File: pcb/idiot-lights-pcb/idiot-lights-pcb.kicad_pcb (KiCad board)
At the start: 2 copper layers, 100.3 x 66 mm, 49 parts, among them SW1 Toggle left indicator, SW2 Toggle right indicator, SW3 Toggle hazard warning, SW4 Break control, SW5 Reset, U1 RaspberryPi_Pico

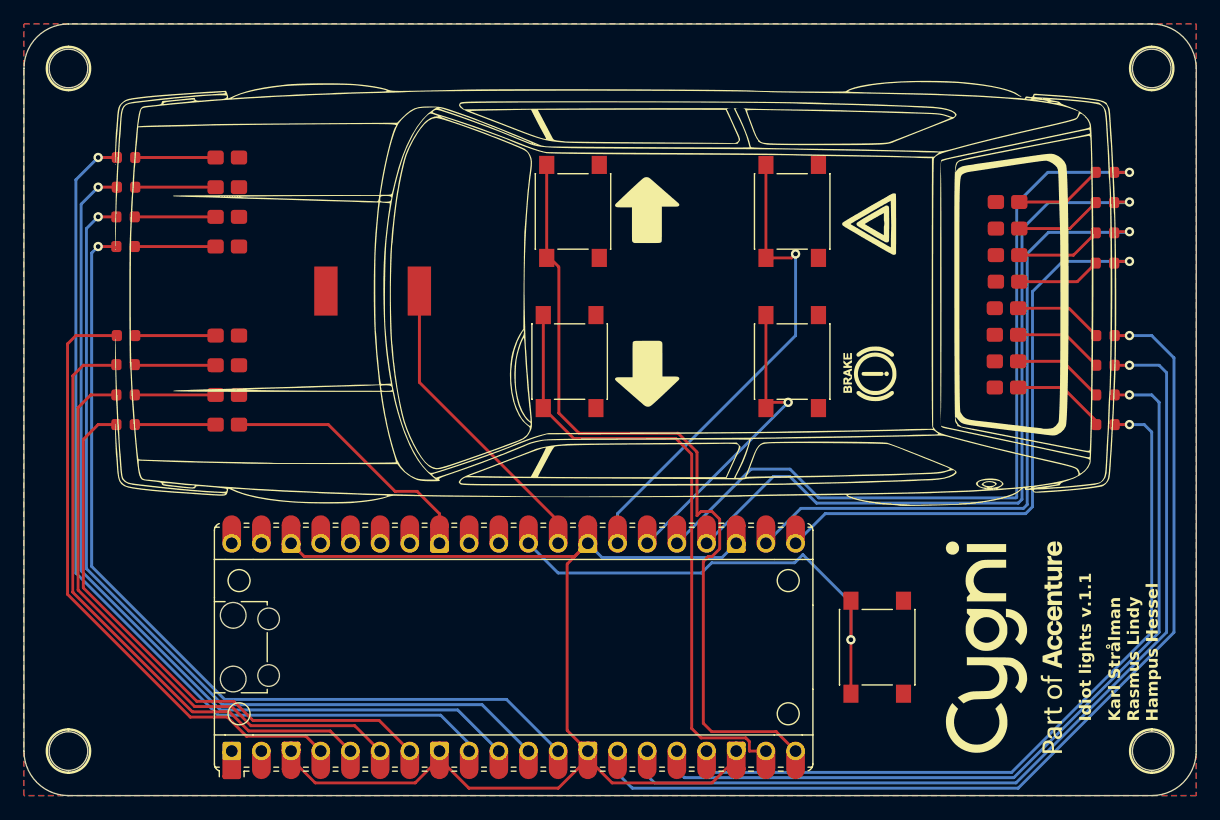
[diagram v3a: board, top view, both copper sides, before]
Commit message: Add mosfet controlling every LED and let 5V rail handle powering
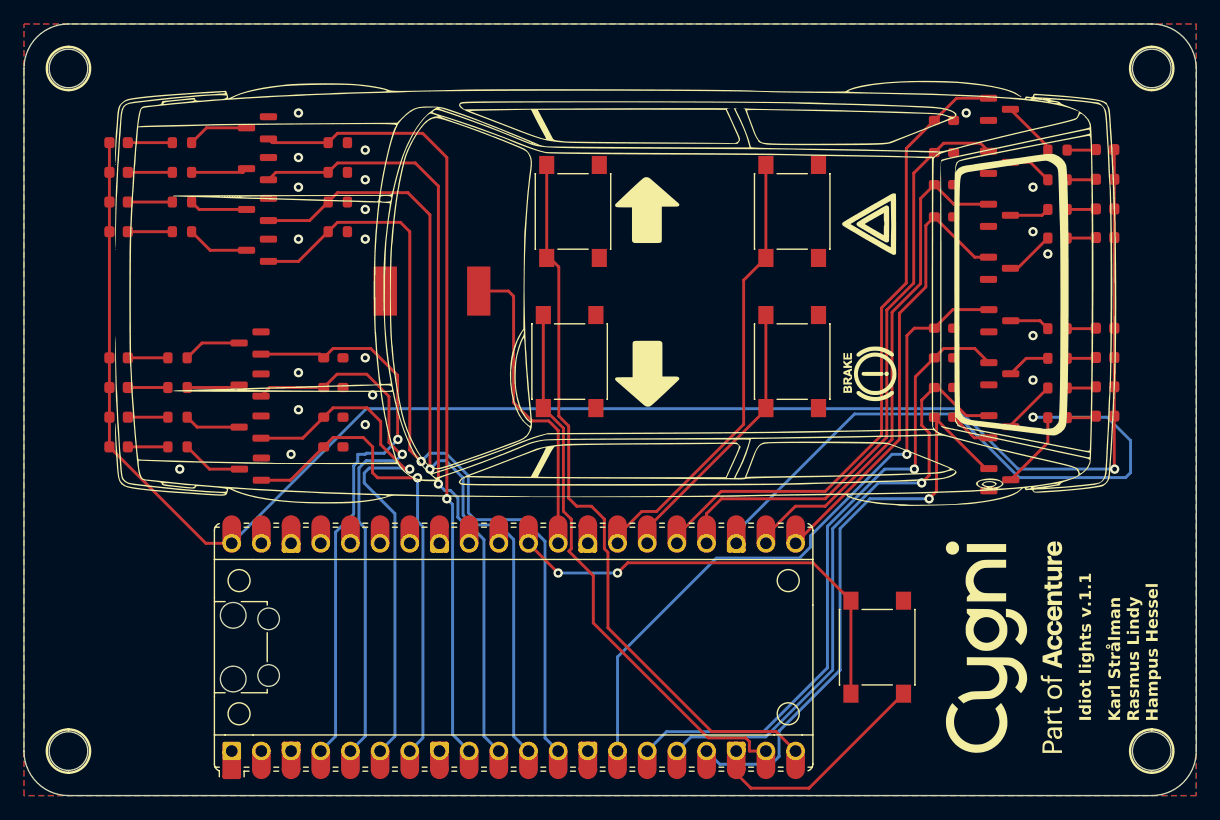
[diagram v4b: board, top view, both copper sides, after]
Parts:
- added Q1: BSS138, Package_TO_SOT_SMD_no_silk:SOT-23_no_silk, F.Cu at (154.0, 64.1)
- added Q10: BSS138, Package_TO_SOT_SMD_no_silk:SOT-23_no_silk, F.Cu at (218.1, 66.8)
- added Q11: BSS138, Package_TO_SOT_SMD_no_silk:SOT-23_no_silk, F.Cu at (218.1, 71.3)
- added Q12: BSS138, Package_TO_SOT_SMD_no_silk:SOT-23_no_silk, F.Cu at (218.1, 75.8)
- added Q13: BSS138, Package_TO_SOT_SMD_no_silk:SOT-23_no_silk, F.Cu at (218.1, 44.1)
- added Q14: BSS138, Package_TO_SOT_SMD_no_silk:SOT-23_no_silk, F.Cu at (218.1, 48.7)
- added Q15: BSS138, Package_TO_SOT_SMD_no_silk:SOT-23_no_silk, F.Cu at (218.1, 53.2)
- added Q16: BSS138, Package_TO_SOT_SMD_no_silk:SOT-23_no_silk, F.Cu at (218.1, 57.7)
- added Q2: BSS138, Package_TO_SOT_SMD_no_silk:SOT-23_no_silk, F.Cu at (154.0, 67.7)
- added Q3: BSS138, Package_TO_SOT_SMD_no_silk:SOT-23_no_silk, F.Cu at (154.0, 71.3)
- added Q4: BSS138, Package_TO_SOT_SMD_no_silk:SOT-23_no_silk, F.Cu at (154.0, 74.9)
- added Q5: BSS138, Package_TO_SOT_SMD_no_silk:SOT-23_no_silk, F.Cu at (154.6, 45.7)
- added Q6: BSS138, Package_TO_SOT_SMD_no_silk:SOT-23_no_silk, F.Cu at (154.6, 49.2)
- added Q7: BSS138, Package_TO_SOT_SMD_no_silk:SOT-23_no_silk, F.Cu at (154.6, 52.7)
- added Q8: BSS138, Package_TO_SOT_SMD_no_silk:SOT-23_no_silk, F.Cu at (154.6, 56.2)
- added Q9: BSS138, Package_TO_SOT_SMD_no_silk:SOT-23_no_silk, F.Cu at (218.1, 62.2)
- added R17: 10k, Resistor_SMD_no_silk:R_0603_1608Metric_no_silk, F.Cu at (213.4, 62.9)
- added R18: 125, Resistor_SMD_no_silk:R_0603_1608Metric_no_silk, F.Cu at (223.1, 62.9)
- added R19: 10k, Resistor_SMD_no_silk:R_0603_1608Metric_no_silk, F.Cu at (213.4, 65.4)
- added R20: 125, Resistor_SMD_no_silk:R_0603_1608Metric_no_silk, F.Cu at (223.1, 65.4)
- added R21: 10k, Resistor_SMD_no_silk:R_0603_1608Metric_no_silk, F.Cu at (213.4, 67.9)
- added R22: 125, Resistor_SMD_no_silk:R_0603_1608Metric_no_silk, F.Cu at (223.1, 68.0)
- added R23: 10k, Resistor_SMD_no_silk:R_0603_1608Metric_no_silk, F.Cu at (213.4, 70.5)
- added R24: 125, Resistor_SMD_no_silk:R_0603_1608Metric_no_silk, F.Cu at (223.1, 70.5)
- added R25: 10k, Resistor_SMD_no_silk:R_0603_1608Metric_no_silk, F.Cu at (213.4, 45.1)
- added R26: 125, Resistor_SMD_no_silk:R_0603_1608Metric_no_silk, F.Cu at (223.1, 47.6)
- added R27: 10k, Resistor_SMD_no_silk:R_0603_1608Metric_no_silk, F.Cu at (213.4, 47.8)
- added R28: 125, Resistor_SMD_no_silk:R_0603_1608Metric_no_silk, F.Cu at (223.1, 50.2)
- added R29: 10k, Resistor_SMD_no_silk:R_0603_1608Metric_no_silk, F.Cu at (213.4, 50.6)
- added R30: 125, Resistor_SMD_no_silk:R_0603_1608Metric_no_silk, F.Cu at (223.1, 52.7)
- added R31: 10k, Resistor_SMD_no_silk:R_0603_1608Metric_no_silk, F.Cu at (213.4, 53.3)
- added R32: 125, Resistor_SMD_no_silk:R_0603_1608Metric_no_silk, F.Cu at (223.1, 55.2)
- R1, R11, R13, R15, R3, R5, R7, R9: value 125 -> 10k; footprint Resistor_SMD:R_0805_2012Metric_Pad1.20x1.40mm_HandSolder -> Resistor_SMD_no_silk:R_0603_1608Metric_no_silk
- R10, R12, R14, R16, R2, R4, R6, R8: footprint Resistor_SMD:R_0805_2012Metric_Pad1.20x1.40mm_HandSolder -> Resistor_SMD_no_silk:R_0603_1608Metric_no_silk
- moved R10 73.0 mm to (148.1, 47.0), turned to 0 degrees
- moved R12 71.5 mm to (148.1, 49.5), turned to 0 degrees
- moved R14 70.8 mm to (148.1, 52.1), turned to 0 degrees
- moved R16 70.7 mm to (148.1, 54.6), turned to 0 degrees
- moved R9 60.9 mm to (161.5, 47.0), turned to 0 degrees
- moved R11 58.9 mm to (161.5, 49.5), turned to 0 degrees
- moved R13 57.7 mm to (161.5, 52.1), turned to 0 degrees
- moved R15 57.3 mm to (161.5, 54.6), turned to 0 degrees
- moved R8 25.1 mm to (147.8, 73.0)
- moved R7 24.0 mm to (161.1, 73.0)
- moved R6 17.7 mm to (147.8, 70.5)
- moved R5 17.2 mm to (161.1, 70.5)
- moved R1 10.7 mm to (161.1, 65.4)
- moved D13 9.72 mm to (227.1, 47.6)
- moved D4 9.55 mm to (142.7, 73.0)
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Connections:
- D1 pad 2: /FL3 -> +5V
- D10 pad 2: /RL2 -> +5V
- D11 pad 2: /RL1 -> +5V
- D12 pad 2: /RL0 -> +5V
- D13 pad 2: /RR3 -> +5V
- D14 pad 2: /RR2 -> +5V
- D15 pad 2: /RR1 -> +5V
- D16 pad 2: /RR0 -> +5V
- D2 pad 2: /FL2 -> +5V
- D3 pad 2: /FL1 -> +5V
- D4 pad 2: /FL0 -> +5V
- D5 pad 2: /FR3 -> +5V
- D6 pad 2: /FR2 -> +5V
- D7 pad 2: /FR1 -> +5V
- D8 pad 2: /FR0 -> +5V
- D9 pad 2: /RL3 -> +5V
- R1 pad 1: Net-(D1-K) -> /FL0
- R10 pad 1: Net-(D10-K) -> Net-(D5-K)
- R10 pad 2: GND -> Net-(Q5-D)
- R11 pad 1: Net-(D11-K) -> /FR1
- R12 pad 1: Net-(D12-K) -> Net-(D6-K)
- R12 pad 2: GND -> Net-(Q6-D)
- R13 pad 1: Net-(D13-K) -> /FR2
- R14 pad 1: Net-(D14-K) -> Net-(D7-K)
- R14 pad 2: GND -> Net-(Q7-D)
- R15 pad 1: Net-(D15-K) -> /FR3
- R16 pad 1: Net-(D16-K) -> Net-(D8-K)
- R16 pad 2: GND -> Net-(Q8-D)
- R2 pad 1: Net-(D2-K) -> Net-(D1-K)
- R2 pad 2: GND -> Net-(Q1-D)
- R3 pad 1: Net-(D3-K) -> /FL1
- R4 pad 1: Net-(D4-K) -> Net-(D2-K)
- R4 pad 2: GND -> Net-(Q2-D)
- R5 pad 1: Net-(D5-K) -> /FL2
- R6 pad 1: Net-(D6-K) -> Net-(D3-K)
- R6 pad 2: GND -> Net-(Q3-D)
- R7 pad 1: Net-(D7-K) -> /FL3
- R8 pad 1: Net-(D8-K) -> Net-(D4-K)
- R8 pad 2: GND -> Net-(Q4-D)
- R9 pad 1: Net-(D9-K) -> /FR0
- U1 pad 13: Net-(U1-GND-Pad13) -> GND
- U1 pad 18: Net-(U1-GND-Pad13) -> GND
- U1 pad 23: Net-(U1-GND-Pad13) -> GND
- U1 pad 28: Net-(U1-GND-Pad13) -> GND
- U1 pad 3: Net-(U1-GND-Pad13) -> GND
- U1 pad 33: GND -> unconnected-(U1-AGND-Pad33)
- U1 pad 38: Net-(U1-GND-Pad13) -> GND
- U1 pad 40: unconnected-(U1-VBUS-Pad40) -> +5V
- U1 pad 8: Net-(U1-GND-Pad13) -> GND
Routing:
- net +5V: track 0.00 -> 149.8 mm, vias 0 -> 1
- net Net-(U1-GND-Pad13): track 105.5 -> 0.00 mm
- net GND: track 22.9 -> 77.1 mm, vias 0 -> 22
- net /RL0: track 84.9 -> 58.7 mm
- net /RL1: track 79.1 -> 55.7 mm
- net /RL2: track 72.1 -> 52.4 mm
- net /RR0: track 70.0 -> 55.3 mm, vias 1 -> 0
- net /RL3: track 65.1 -> 50.8 mm
- net /RR1: track 65.1 -> 51.3 mm, vias 1 -> 0
- net /RR2: track 56.1 -> 42.8 mm, vias 1 -> 0
- net /RR3: track 50.7 -> 38.9 mm, vias 1 -> 0
- net /FR1: track 77.2 -> 66.9 mm
- net /FR0: track 78.3 -> 68.2 mm
- net /FR2: track 76.4 -> 68.1 mm
- net /FL3: track 49.8 -> 41.7 mm, vias 0 -> 1
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
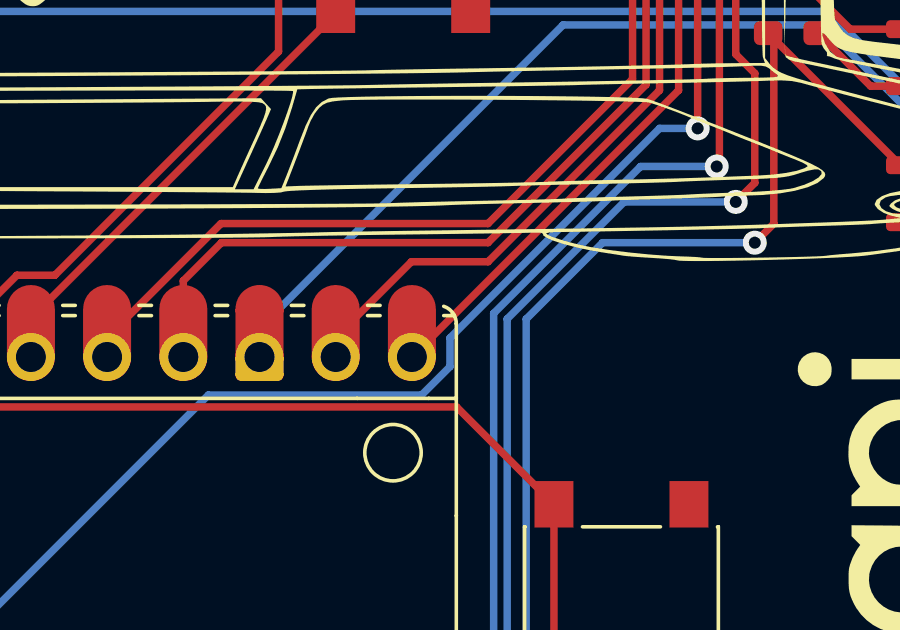
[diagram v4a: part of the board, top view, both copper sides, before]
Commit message: Add MPN field and generate bom
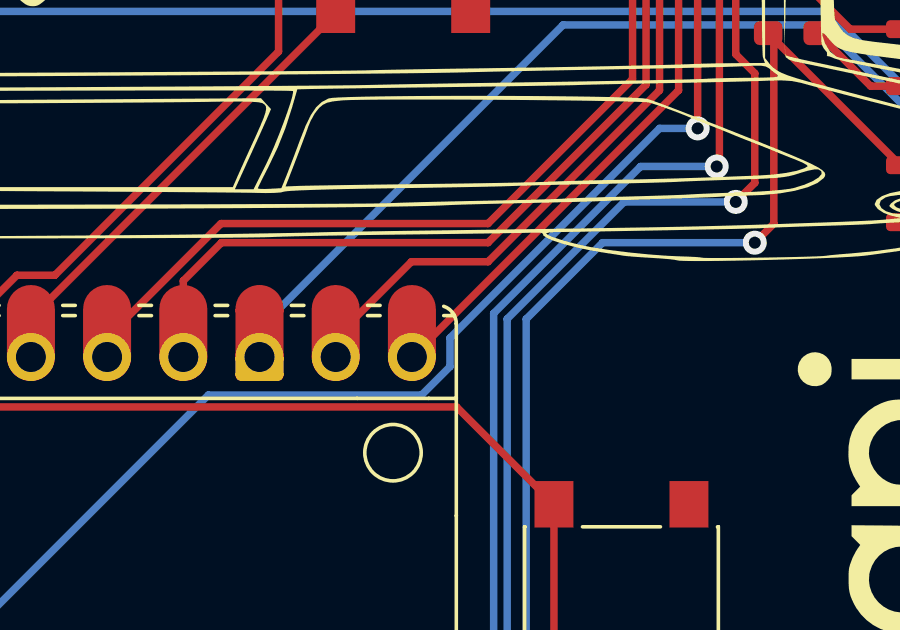
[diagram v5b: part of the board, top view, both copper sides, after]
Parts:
- R10, R12, R14, R16, R18, R2, R20, R22, R24, R26, R28, R30, R32, R4, R6, R8: value 125 -> 150

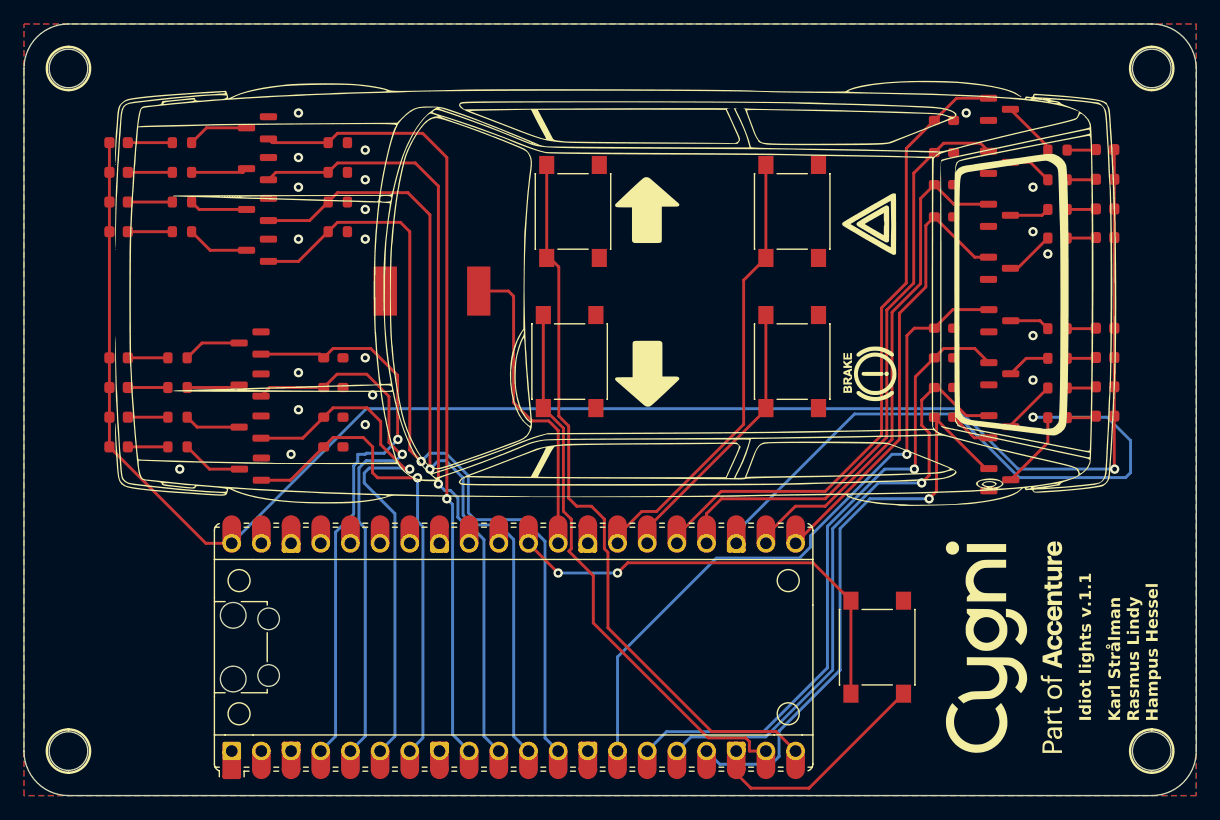
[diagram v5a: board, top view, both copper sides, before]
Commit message: Replace car silk with free model
Source https://www.freecads.com/en/transportation/car-top-view-00000998
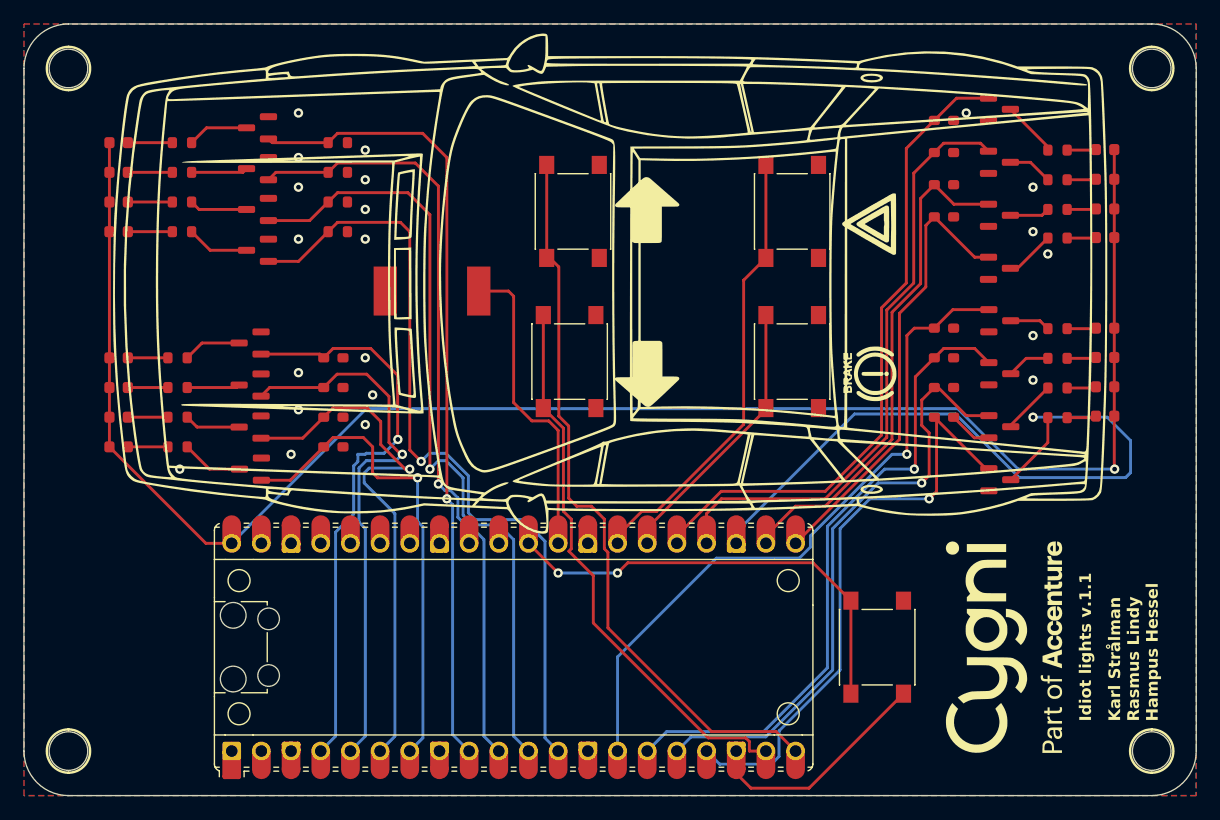
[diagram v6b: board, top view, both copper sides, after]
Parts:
- removed the G*** at (185.4, 59.7)
- added G***: LOGO, Telltale_icons:car, F.Cu at (184.8, 59.1)

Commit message: Add github link QR code on B.Silk
Remove rearview mirror on car (too bulky)

Fix project paths
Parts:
- added G***: LOGO, cts-qr-code:qr, B.Cu at (185.4, 70.5)
- moved G*** 13.4 mm to (174.6, 51.4)
- moved G*** 13.4 mm to (174.6, 67.9)
- moved G*** 13.4 mm to (193.7, 53.3)
- moved G*** 13.4 mm to (193.7, 66.0)
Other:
- board text added: "Reset"
- board text added: "cts2023-turn-cygnicator"
- board text added: "turn-cygnicator v.1.1"
- board text removed: "Idiot lights v.1.1"
